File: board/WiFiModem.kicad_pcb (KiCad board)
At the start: 2 copper layers, 88.9 x 61 mm, 49 parts, among them J1 DB9_Female, J2 DB25_Female, J3 Barrel_Jack_Switch, J4 PRG, SW1 SW_Push, SW2 SW_Push, U1 ESP-12E, U2 LM7805_TO220, U3 MAX232, U4 LT1117-3.3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

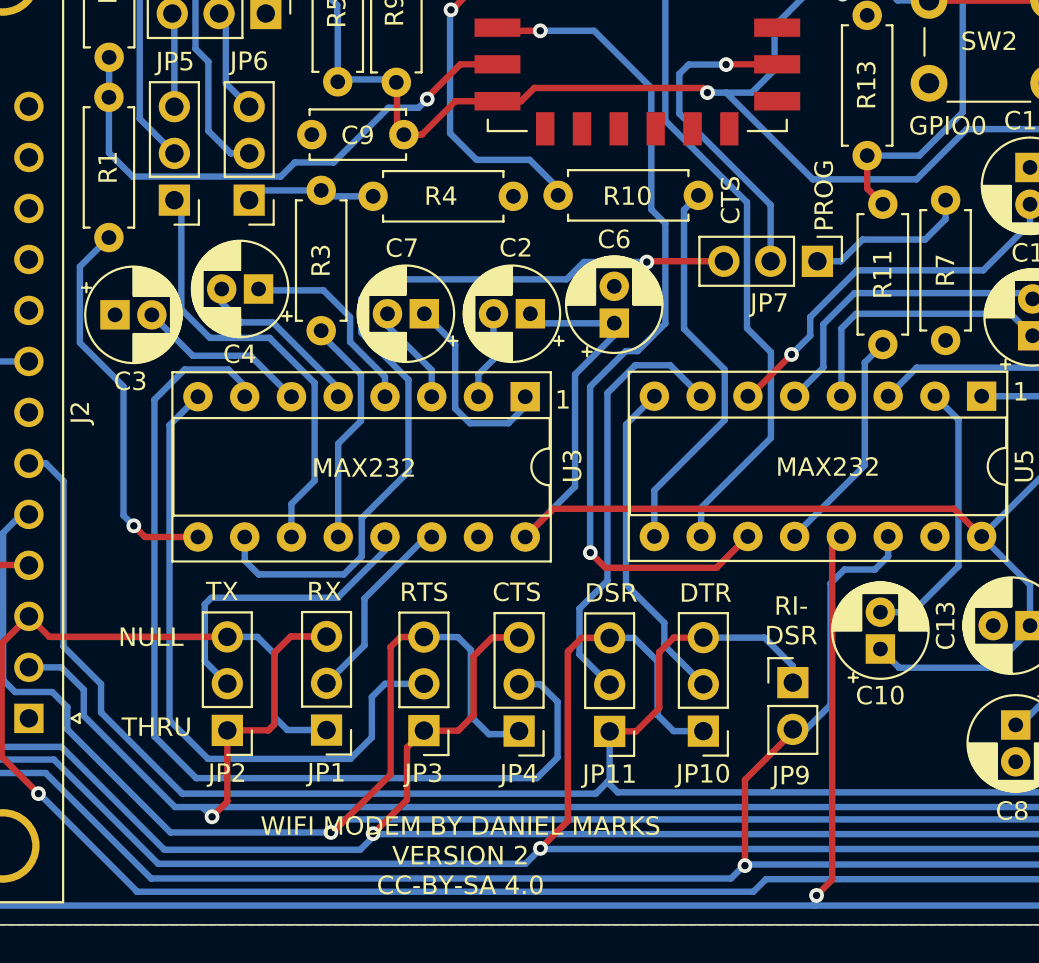
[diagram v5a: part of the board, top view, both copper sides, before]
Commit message: Fixed GPIO15 booting issue, changed DCD/DSR/DTR jumper
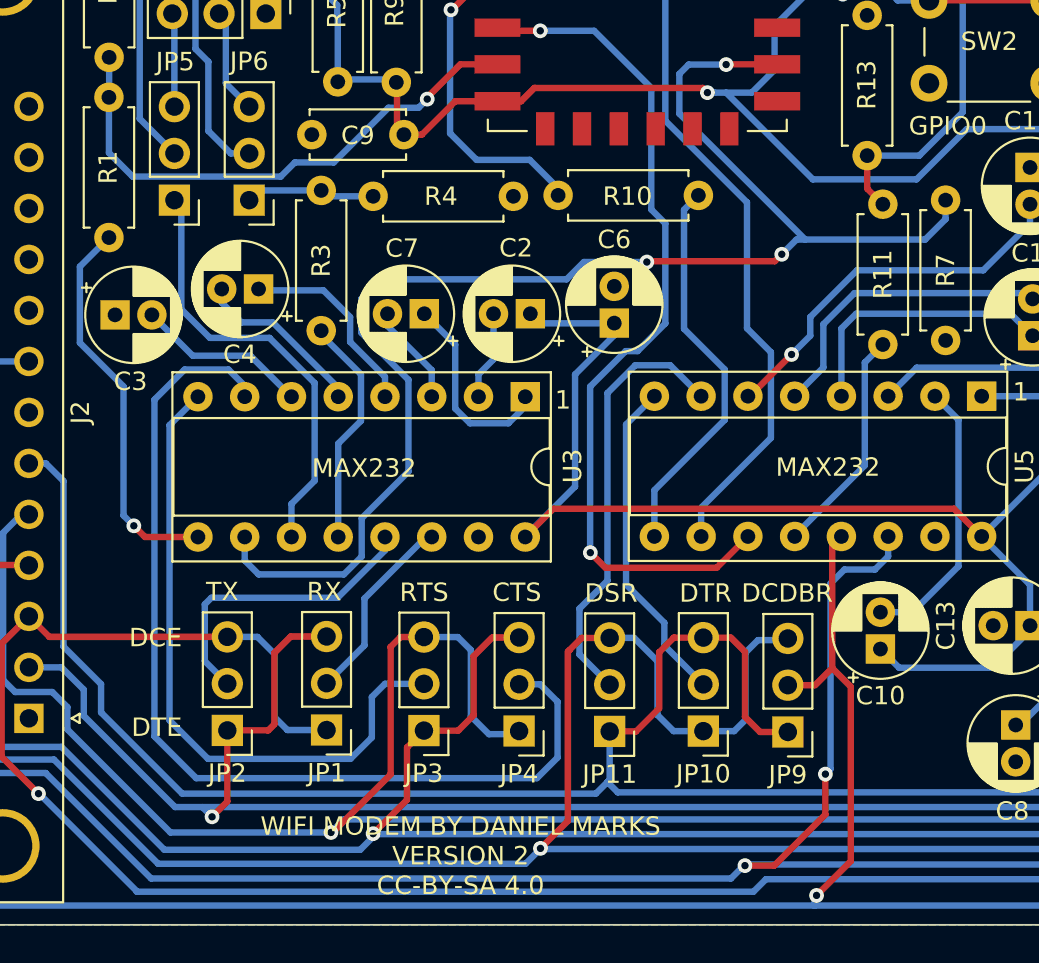
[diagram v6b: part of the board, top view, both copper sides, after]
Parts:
- removed JP7: PROG, Connector_PinHeader_2.54mm:PinHeader_1x03_P2.54mm_Vertical
- JP11: value DTRB -> DSRB
- JP9: value RIDSR -> DCDBRIDGE; footprint Connector_PinHeader_2.54mm:PinHeader_1x02_P2.54mm_Vertical -> Connector_PinHeader_2.54mm:PinHeader_1x03_P2.54mm_Vertical
- moved JP9 2.69 mm to (123.8, 116.5), turned to 180 degrees
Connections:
- JP9 pad 2: RI -> DCD
- R7 pad 1: Net-(JP7-Pad1) -> GPIO15
- U1 pad 16: Net-(JP7-Pad2) -> GPIO15
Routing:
- net GPIO15: track 45.0 -> 76.4 mm, vias 1 -> 3
- net Net-(JP7-Pad2): track 17.8 -> 0.00 mm, vias 1 -> 0
- net Net-(JP7-Pad1): track 8.94 -> 0.00 mm
- net DTR: track 129.3 -> 138.1 mm
- net DCD: track 164.4 -> 168.1 mm
- net DSR: track 116.0 -> 118.4 mm
- net RI: track 137.1 -> 137.6 mm, vias 2 -> 3
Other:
- board text added: "DCDBR"
- board text added: "DCE"
- board text added: "DTE"
- board text removed: "NULL"
- board text removed: "PROG"
- board text removed: "RI- DSR"
- board text removed: "THRU"

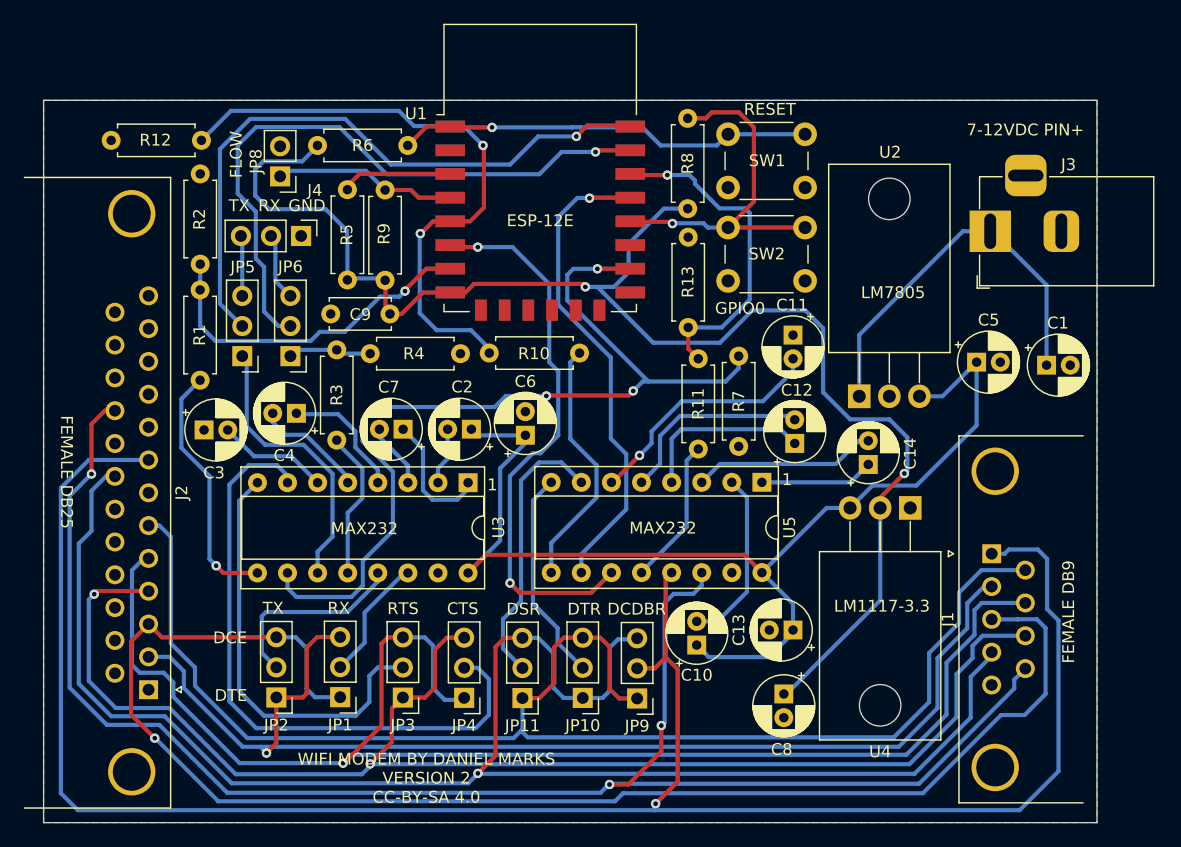
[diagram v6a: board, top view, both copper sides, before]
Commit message: Fixed DCD and DB25 pinouts
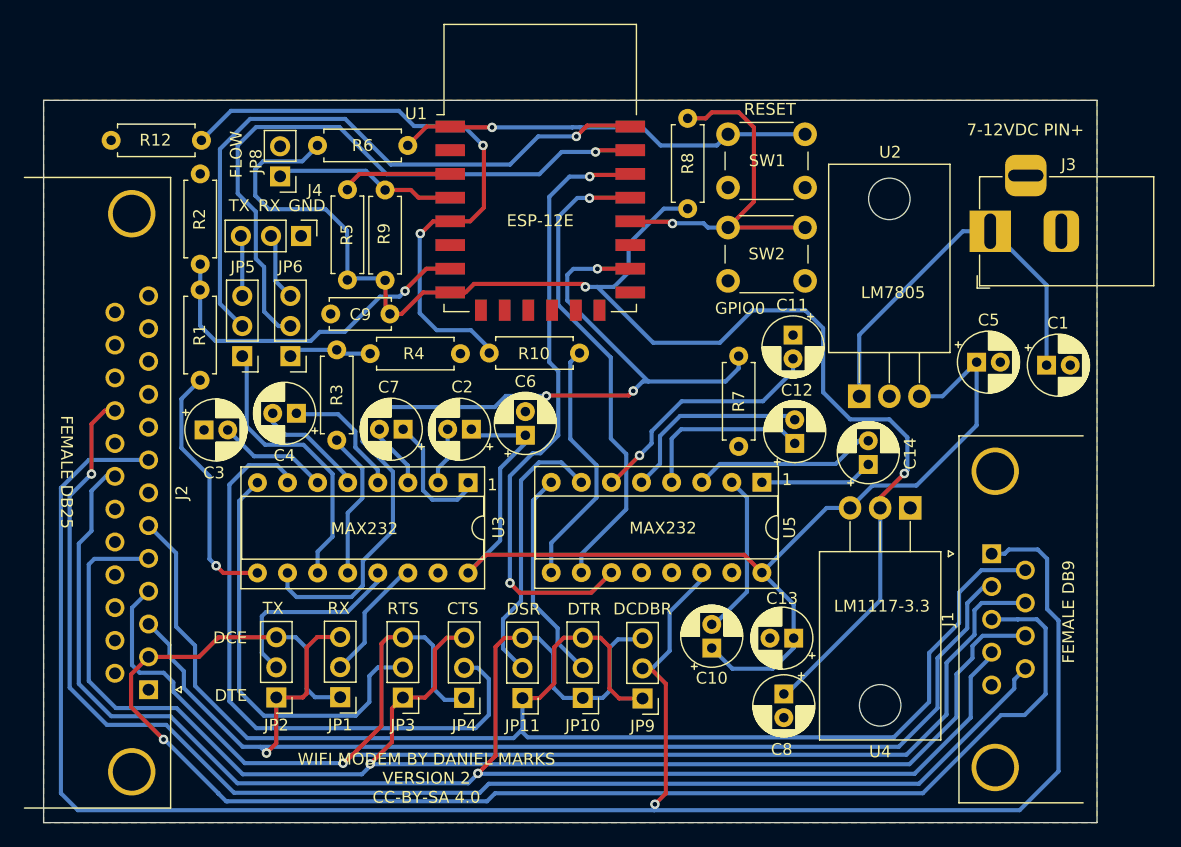
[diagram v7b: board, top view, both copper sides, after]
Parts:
- removed R11: 470R, Resistor_THT:R_Axial_DIN0207_L6.3mm_D2.5mm_P7.62mm_Horizontal
- removed R13: 1k, Resistor_THT:R_Axial_DIN0207_L6.3mm_D2.5mm_P7.62mm_Horizontal
- moved C10 1.30 mm to (130.0, 112.3)
- moved C13 0.69 mm to (137.0, 111.4)
- moved JP9 0.46 mm to (124.2, 116.5)
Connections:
- J2 pad 2: TXD -> RXD
- J2 pad 3: RXD -> TXD
- J2 pad 4: RTS -> CTS
- J2 pad 5: CTS -> RTS
- U5 pad 11: GPIO12 -> GPIO5
- U5 pad 12: Net-(R11-Pad1) -> unconnected-(U5-Pad12)
- U5 pad 13: DCD -> unconnected-(U5-Pad13)
- U5 pad 14: RI -> DCD
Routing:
- net GPIO12: track 47.0 -> 0.00 mm, vias 2 -> 0
- net GPIO5: track 28.1 -> 52.2 mm, vias 1 -> 2
- net RI: track 137.6 -> 114.6 mm, vias 3 -> 1
- net Net-(R11-Pad1): track 12.4 -> 0.00 mm
- net CTS: track 121.8 -> 118.5 mm
- net RXD: track 123.4 -> 120.5 mm
- net RTS: track 118.0 -> 120.9 mm, vias 2 -> 1
- net TXD: track 100.0 -> 101.7 mm
- net Net-(C10-Pad2): track 15.0 -> 13.9 mm

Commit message: Moved around some traces
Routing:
- net DSR: track 118.3 -> 120.2 mm
- net TXD: track 101.7 -> 103.3 mm
- net DCD: track 168.0 -> 166.6 mm
- net RXD: track 120.5 -> 119.4 mm
- net CTS: track 118.5 -> 119.4 mm
- net RTS: track 120.9 -> 121.5 mm
